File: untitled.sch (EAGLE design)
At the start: 26 parts, among them IC1 SN65220DBV, J3 CORTEX_DEBUG_PTH, J4 2X6 FEMALE, J6 USB-MICROB, U1 ATSAMD21G-M, U2 MIC5501-3.0YM5-TR, Y1 32.768kHz

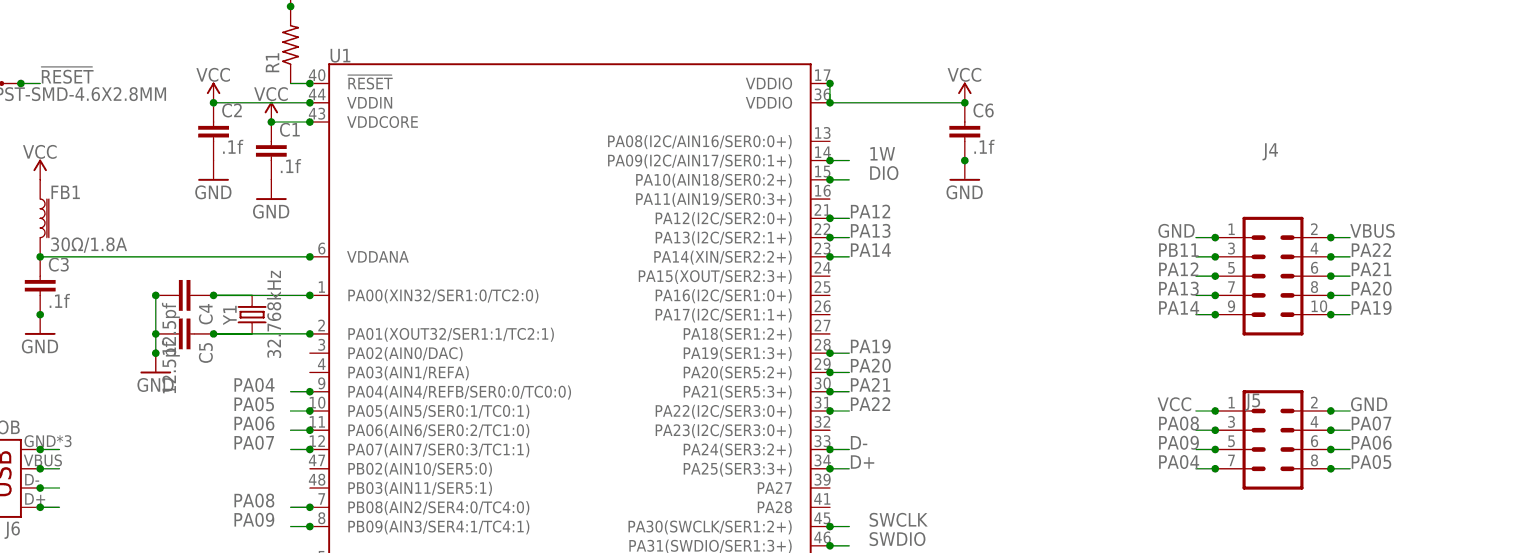
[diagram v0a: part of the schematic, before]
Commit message: corrected button orientation
placed novelkey on the correct side. reduced gpio by 2 pins to allow for tolerances. added mounting hole. updated routing.
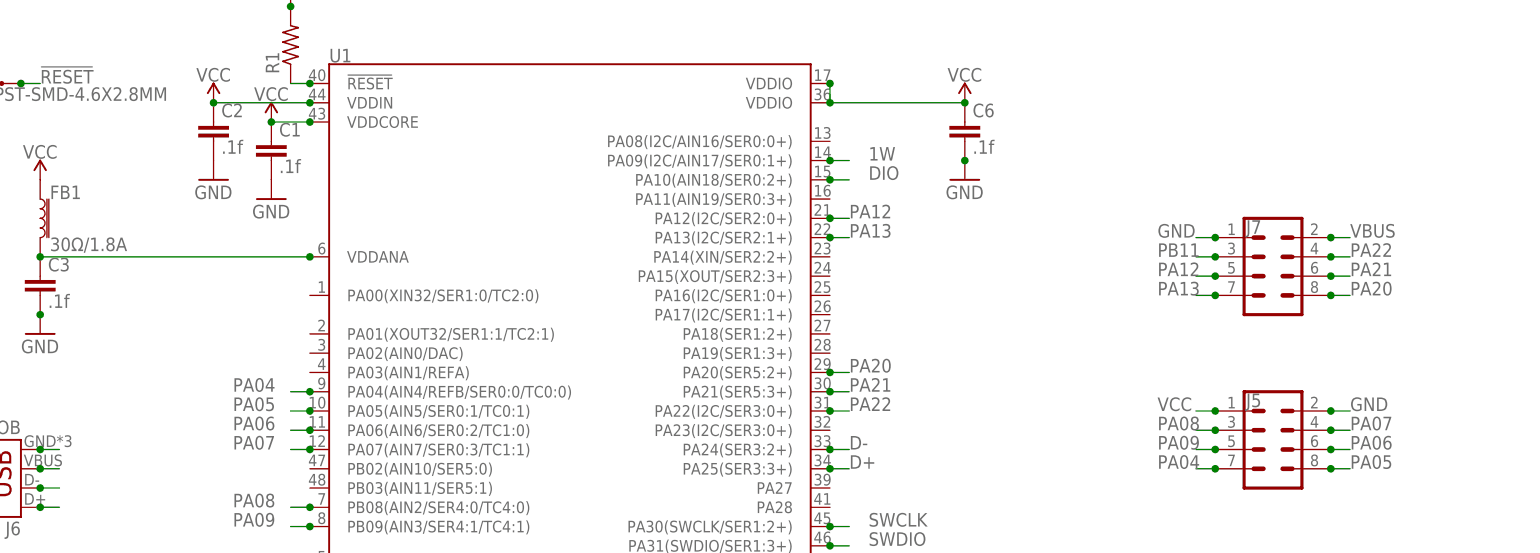
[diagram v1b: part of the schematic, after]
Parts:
- removed C4, C5: 12.5pf, resistor:C-EUC0402
- removed J4: 2X6 FEMALE, SparkFun-Connectors:CONN_05X2PTH
- removed Y1: 32.768kHz, SparkFun-Clocks-custom:CRYSTAL-32.768KHZSMD-3.2X1.5
- added J7: (no value), SparkFun-Connectors:CONN_04X2
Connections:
- removed net N$5: C4.1, U1.PA00(XIN32/SER1:0/TC2:0), Y1.2
- removed net N$6: C5.1, U1.PA01(XOUT32/SER1:1/TC2:1), Y1.1
- removed net PA14: J4.9, U1.PA14(XIN/SER2:2+)
- removed net PA19: J4.10, U1.PA19(SER1:3+)
- net GND: now also J7.1; no longer C4.2, C5.2, J4.1
- net PA12: now also J7.5; no longer J4.5
- net PA13: now also J7.7; no longer J4.7
- net PA20: now also J7.8; no longer J4.8
- net PA21: now also J7.6; no longer J4.6
- net PA22: now also J7.4; no longer J4.4
- net PB11: now also J7.3; no longer J4.3
- net VBUS: now also J7.2; no longer J4.2

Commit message: updated silkscreen
updated silkscreen
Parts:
- R1: value (none) -> 10k
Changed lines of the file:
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@@
 <part name="U$2" library="1wire" deviceset="DS2413" device="P"/>
 <part name="U1" library="SparkFun-IC-Microcontroller" library_urn="urn:adsk.eagle:library:525" deviceset="ATSAMD21G" device="-M" package3d_urn="urn:adsk.eagle:package:38962/1"/>
-<part name="R1" library="rcl" library_urn="urn:adsk.eagle:library:334" deviceset="R-US_" device="R0402" package3d_urn="urn:adsk.eagle:package:23547/2"/>
+<part name="R1" library="rcl" library_urn="urn:adsk.eagle:library:334" deviceset="R-US_" device="R0402" package3d_urn="urn:adsk.eagle:package:23547/2" value="10k"/>
 <part name="SUPPLY1" library="SparkFun-PowerSymbols" library_urn="urn:adsk.eagle:library:530" deviceset="VCC" device=""/>
 <part name="C1" library="resistor" library_urn="urn:adsk.eagle:library:348" deviceset="C-EU" device="C0402" package3d_urn="urn:adsk.eagle:package:26136/1" value=".1f"/>

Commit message: added esp version and removed led
added an esp8266 version of the board. Removed an LED from the samd21g version to move the LED to the empty space on the bottom of the novelkey.
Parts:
- removed D1: WS2812B, SparkFun-LED:WS2812B
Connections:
- removed net N$11: D1.DO, D2.DI
- net 5V: no longer D1.VDD
- net DIO: now also D2.DI; no longer D1.DI
- net GND: no longer D1.VSS
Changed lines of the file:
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@@
 <part name="J1" library="SparkFun-Connectors" library_urn="urn:adsk.eagle:library:513" deviceset="CONN_04" device="SMD2" package3d_urn="urn:adsk.eagle:package:38096/1"/>
 <part name="J2" library="SparkFun-Connectors" library_urn="urn:adsk.eagle:library:513" deviceset="CONN_04" device="SMD2" package3d_urn="urn:adsk.eagle:package:38096/1"/>
-<part name="D1" library="SparkFun-LED" library_urn="urn:adsk.eagle:library:529" deviceset="WS2812B" device="" package3d_urn="urn:adsk.eagle:package:39369/1" value="WS2812B"/>
 <part name="D2" library="SparkFun-LED" library_urn="urn:adsk.eagle:library:529" deviceset="WS2812B" device="" package3d_urn="urn:adsk.eagle:package:39369/1" value="WS2812B"/>
 <part name="J6" library="SparkFun-Retired" library_urn="urn:adsk.eagle:library:533" deviceset="USB" device="-MICROB"/>
@@
 <part name="SUPPLY5" library="SparkFun-PowerSymbols" library_urn="urn:adsk.eagle:library:530" deviceset="VCC" device=""/>
 <part name="GND9" library="supply1" library_urn="urn:adsk.eagle:library:371" deviceset="GND" device=""/>
-<part name="GND10" library="supply1" library_urn="urn:adsk.eagle:library:371" deviceset="GND" device=""/>
 <part name="IC1" library="sn65220_40" deviceset="SN65220" device="DBV"/>
 <part name="GND11" library="supply1" library_urn="urn:adsk.eagle:library:371" deviceset="GND" device=""/>
@@
 <attribute name="NAME" x="121.92" y="68.072" size="1.778" layer="95" font="vector" rot="R180"/>
 </instance>
-<instance part="D1" gate="G$1" x="10.16" y="88.9" smashed="yes">
-<attribute name="NAME" x="-2.54" y="97.282" size="1.778" layer="95"/>
-<attribute name="VALUE" x="-2.54" y="81.28" size="1.778" layer="95"/>
-</instance>
 <instance part="D2" gate="G$1" x="10.16" y="66.04" smashed="yes">
 <attribute name="NAME" x="-2.54" y="74.422" size="1.778" layer="95"/>
@@
 <instance part="GND9" gate="1" x="-10.16" y="60.96" smashed="yes">
 <attribute name="VALUE" x="-12.7" y="58.42" size="1.778" layer="96"/>
-</instance>
-<instance part="GND10" gate="1" x="-10.16" y="83.82" smashed="yes">
-<attribute name="VALUE" x="-12.7" y="81.28" size="1.778" layer="96"/>
 </instance>
 <instance part="IC1" gate="G$1" x="274.32" y="76.2" smashed="yes">
@@
 </segment>
 <segment>
-<pinref part="D1" gate="G$1" pin="VSS"/>
-<pinref part="GND10" gate="1" pin="GND"/>
-<wire x1="-10.16" y1="86.36" x2="-5.08" y2="86.36" width="0.1524" layer="91"/>
-<junction x="-10.16" y="86.36"/>
-<junction x="-5.08" y="86.36"/>
-</segment>
-<segment>
 <pinref part="J6" gate="G$1" pin="GND"/>
 <wire x1="124.46" y1="99.06" x2="127" y2="99.06" width="0.1524" layer="91"/>
@@
 </segment>
 <segment>
-<pinref part="D1" gate="G$1" pin="DI"/>
-<wire x1="22.86" y1="93.98" x2="25.4" y2="93.98" width="0.1524" layer="91"/>
-<label x="27.94" y="93.98" size="1.778" layer="95"/>
-<junction x="22.86" y="93.98"/>
-</segment>
-<segment>
 <pinref part="J1" gate="G$1" pin="2"/>
 <wire x1="86.36" y1="73.66" x2="88.9" y2="73.66" width="0.1524" layer="91"/>
@@
 <junction x="86.36" y="73.66"/>
 </segment>
+<segment>
+<pinref part="D2" gate="G$1" pin="DI"/>
+<wire x1="25.4" y1="71.12" x2="22.86" y2="71.12" width="0.1524" layer="91"/>
+<junction x="22.86" y="71.12"/>
+<label x="27.94" y="71.12" size="1.778" layer="95"/>
+</segment>
 </net>
 <net name="N$10" class="0">
@@
 <pinref part="U$1" gate="G$1" pin="P$1"/>
 <junction x="109.22" y="22.86"/>
-</segment>
-</net>
-<net name="N$11" class="0">
-<segment>
-<pinref part="D1" gate="G$1" pin="DO"/>
-<pinref part="D2" gate="G$1" pin="DI"/>
-<wire x1="22.86" y1="86.36" x2="22.86" y2="71.12" width="0.1524" layer="91"/>
-<junction x="22.86" y="86.36"/>
-<junction x="22.86" y="71.12"/>
 </segment>
 </net>
@@
 </segment>
 <segment>
-<pinref part="D1" gate="G$1" pin="VDD"/>
-<wire x1="-10.16" y1="93.98" x2="-5.08" y2="93.98" width="0.1524" layer="91"/>
-<junction x="-5.08" y="93.98"/>
-<label x="-15.24" y="93.98" size="1.778" layer="95"/>
-</segment>
-<segment>

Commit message: added vias below bus connectors
added vias below bus connectors to improve mechanical stability. Added ground symbol on bus connection net.
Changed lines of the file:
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@@
 <part name="J5" library="SparkFun-Connectors" library_urn="urn:adsk.eagle:library:513" deviceset="CONN_04X2" device="" package3d_urn="urn:adsk.eagle:package:38103/1"/>
 <part name="J7" library="SparkFun-Connectors" library_urn="urn:adsk.eagle:library:513" deviceset="CONN_04X2" device="" package3d_urn="urn:adsk.eagle:package:38103/1"/>
+<part name="GND3" library="supply1" library_urn="urn:adsk.eagle:library:371" deviceset="GND" device=""/>
 </parts>
 <sheets>
@@
 <attribute name="NAME" x="283.464" y="127.508" size="1.778" layer="95" font="vector"/>
 <attribute name="VALUE" x="283.718" y="116.078" size="1.778" layer="96" font="vector" align="top-left"/>
+</instance>
+<instance part="GND3" gate="1" x="99.06" y="68.58" smashed="yes">
+<attribute name="VALUE" x="96.52" y="66.04" size="1.778" layer="96"/>
 </instance>
 </instances>
@@
 <pinref part="J1" gate="G$1" pin="1"/>
 <pinref part="J2" gate="G$1" pin="4"/>
-<wire x1="111.76" y1="71.12" x2="86.36" y2="71.12" width="0.1524" layer="91"/>
+<wire x1="111.76" y1="71.12" x2="99.06" y2="71.12" width="0.1524" layer="91"/>
 <junction x="86.36" y="71.12"/>
 <junction x="111.76" y="71.12"/>
 <label x="86.36" y="71.12" size="1.778" layer="95"/>
-</segment>
-<segment>
+<pinref part="GND3" gate="1" pin="GND"/>
+<wire x1="99.06" y1="71.12" x2="86.36" y2="71.12" width="0.1524" layer="91"/>
+<junction x="99.06" y="71.12"/>
+</segment>
+<segment>

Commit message: changed button from 3v to 5v
moved button from 3v to 5v as the ds2413 is 5v tolerant and 5v is passed via the bus connector while 3v is not. Also negates the need for a vreg on each board.
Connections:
- net 5V: now also U$1.P$2
- net VCC: no longer U$1.P$2
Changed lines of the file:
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@@
 <part name="S2" library="SparkFun-Switches" library_urn="urn:adsk.eagle:library:535" deviceset="MOMENTARY-SWITCH-SPST" device="-SMD-4.6X2.8MM" package3d_urn="urn:adsk.eagle:package:40176/1"/>
 <part name="R2" library="rcl" library_urn="urn:adsk.eagle:library:334" deviceset="R-US_" device="R0402" package3d_urn="urn:adsk.eagle:package:23547/2" value="4.7k"/>
-<part name="SUPPLY5" library="SparkFun-PowerSymbols" library_urn="urn:adsk.eagle:library:530" deviceset="VCC" device=""/>
 <part name="GND9" library="supply1" library_urn="urn:adsk.eagle:library:371" deviceset="GND" device=""/>
 <part name="IC1" library="sn65220_40" deviceset="SN65220" device="DBV"/>
@@
 <attribute name="VALUE" x="122.682" y="41.91" size="1.778" layer="96" rot="R90"/>
 </instance>
-<instance part="SUPPLY5" gate="G$1" x="139.7" y="22.86" smashed="yes">
-<attribute name="VALUE" x="139.7" y="25.654" size="1.778" layer="96" align="bottom-center"/>
-</instance>
 <instance part="GND9" gate="1" x="-10.16" y="60.96" smashed="yes">
 <attribute name="VALUE" x="-12.7" y="58.42" size="1.778" layer="96"/>
@@
 <junction x="246.38" y="144.78"/>
 <junction x="228.6" y="147.32"/>
-</segment>
-<segment>
-<pinref part="U$1" gate="G$1" pin="P$2"/>
-<pinref part="SUPPLY5" gate="G$1" pin="VCC"/>
-<junction x="139.7" y="22.86"/>
 </segment>
 <segment>
@@
 <label x="-15.24" y="71.12" size="1.778" layer="95"/>
 </segment>
-</net>
+<segment>
+<pinref part="U$1" gate="G$1" pin="P$2"/>
+<wire x1="139.7" y1="22.86" x2="142.24" y2="22.86" width="0.1524" layer="91"/>
+<label x="142.24" y="22.86" size="1.778" layer="95"/>
+<junction x="139.7" y="22.86"/>
+</segment>
+</net>

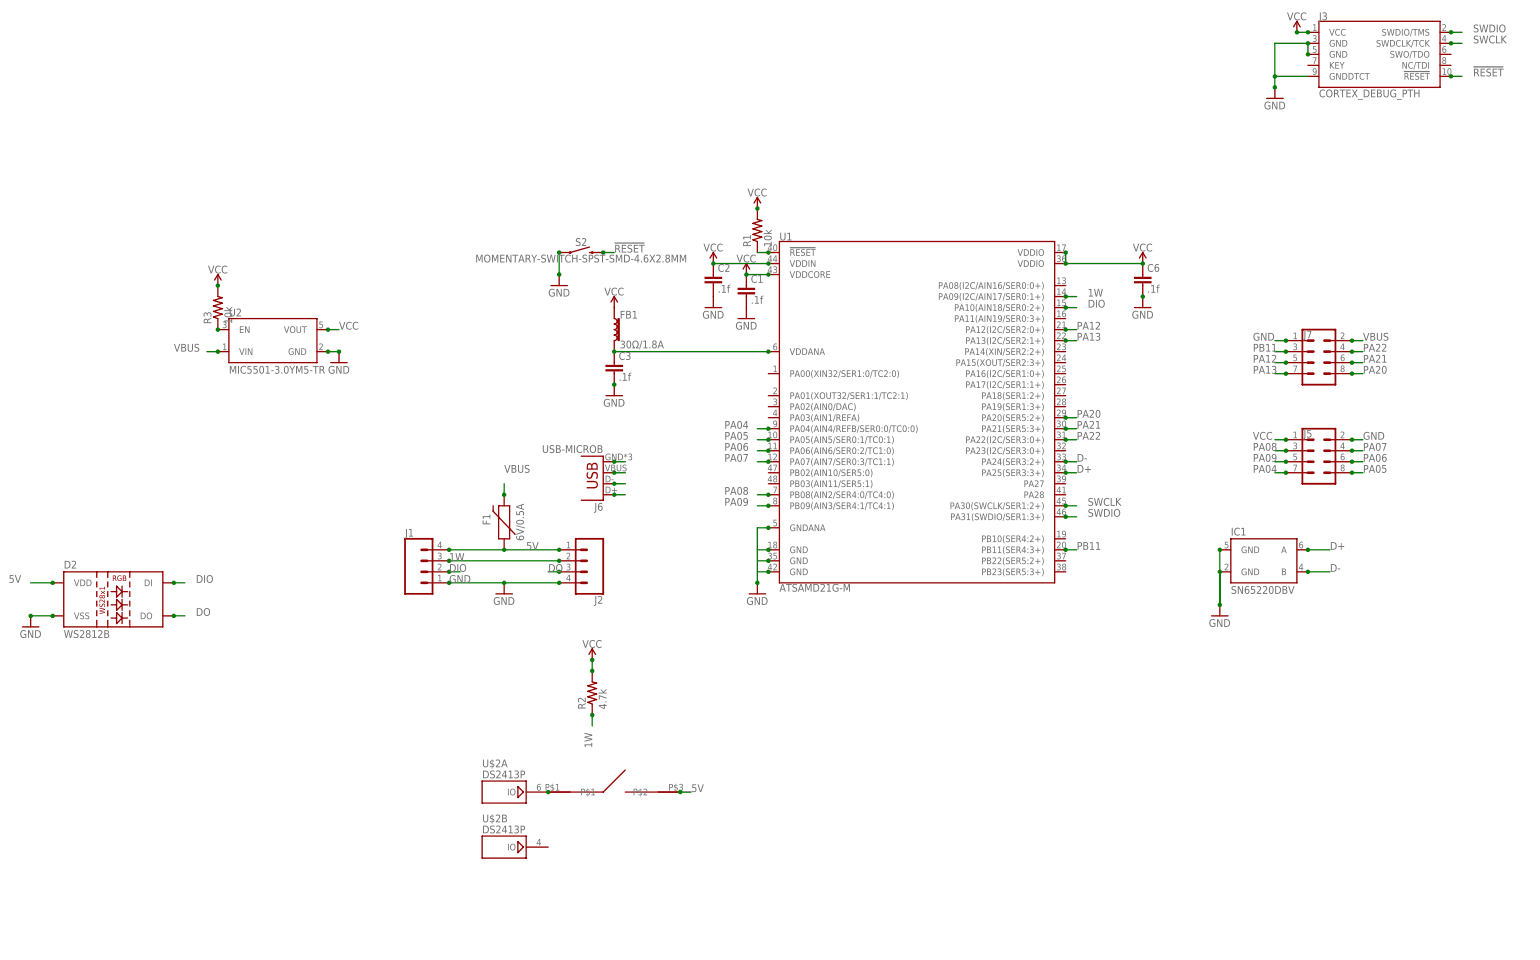
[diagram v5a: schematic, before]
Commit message: Rev 1 error fixes
Updated ldo pull up resistor to Vin. Moved part values to layer that will show up in silkscreen. Updated capacitor footprint to match proper 0402 sizing. Replaced usb tvs/res IC. increased pullback.
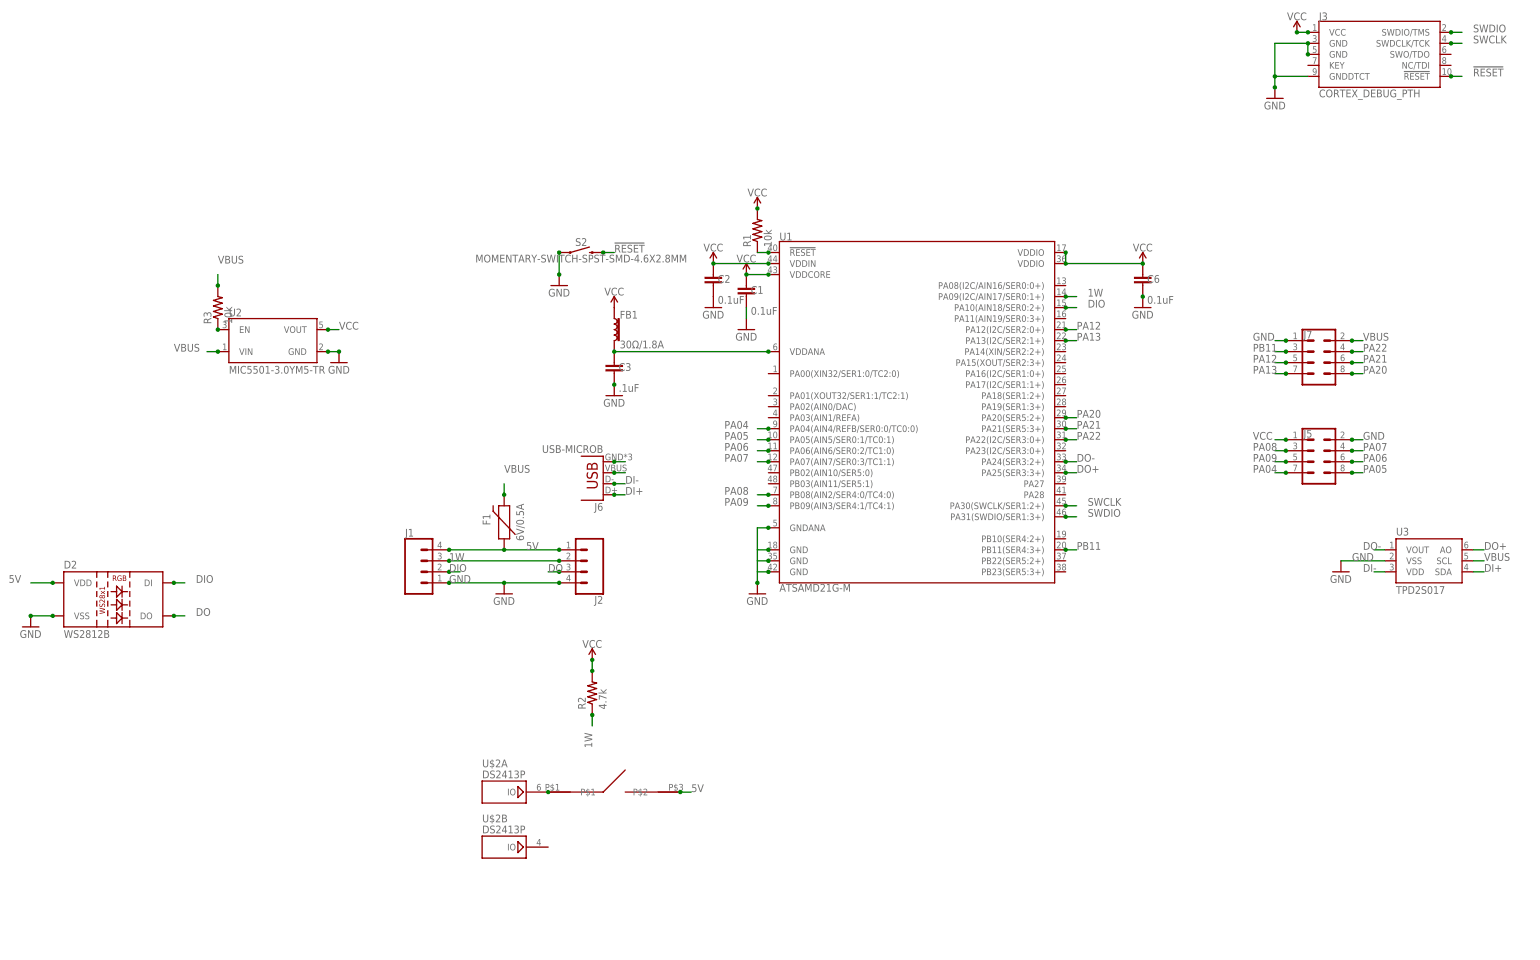
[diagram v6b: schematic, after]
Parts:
- removed IC1: SN65220DBV, sn65220_40:SN65220DBV
- added U3: TPD2S017, SparkFun-IC-Conversion:MCP4725SOT-23
- C1, C2, C6: value .1f -> 0.1uF; device resistor:C-EUC0402 -> SparkFun-Capacitors:0.1UF-0402-16V-10%
- C3: value .1f -> .1uF; device resistor:C-EUC0402 -> SparkFun-Capacitors:0.1UF-0402-16V-10%
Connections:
- removed net D+: IC1.A, J6.D+, U1.PA25(SER3:3+)
- removed net D-: IC1.B, J6.D-, U1.PA24(SER3:2+)
- new net DI+: J6.D+, U3.SDA
- new net DI-: J6.D-, U3.VDD
- new net DO+: U1.PA25(SER3:3+), U3.AO
- new net DO-: U1.PA24(SER3:2+), U3.VOUT
- net GND: now also U3.VSS; no longer IC1.GND@1, IC1.GND@2
- net VBUS: now also R3.2, U3.SCL
- net VCC: no longer R3.2
